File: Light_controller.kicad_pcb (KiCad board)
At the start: 2 copper layers, 42 parts, among them U1 LM358, U10 PH2.0_horizontal, U11 PH2.0_horizontal, U12 PH2.0_horizontal, U13 PinSocket_1x4, U14 SMD2063, U2 PT8211-S, U3 STM8S003F3P, U4 SMD_2062, U5 tact_sw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

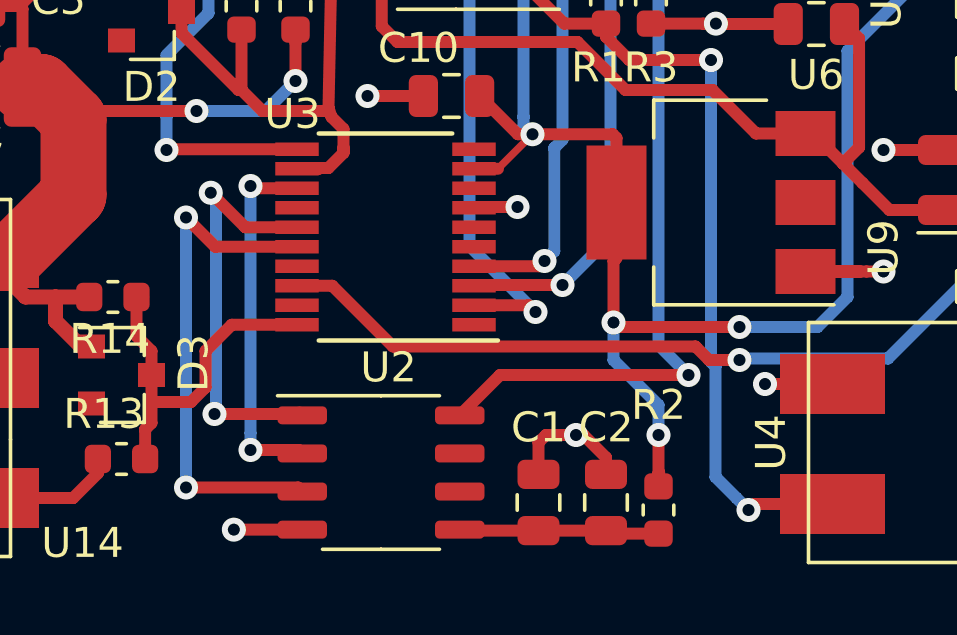
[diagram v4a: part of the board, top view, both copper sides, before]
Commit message: updated layout
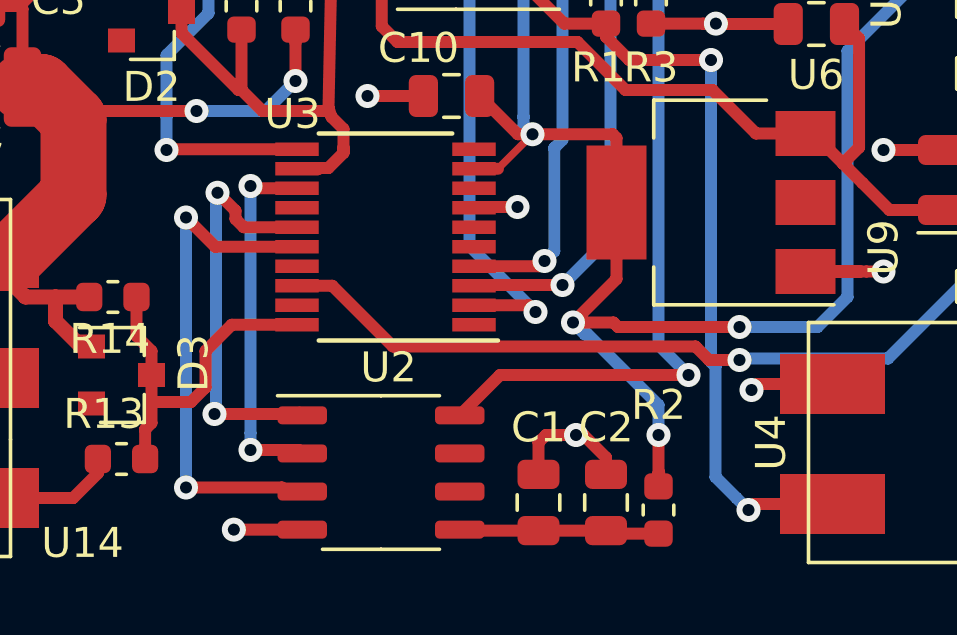
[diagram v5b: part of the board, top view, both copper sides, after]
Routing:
- net /5V_SUPPLY: track 101.5 -> 106.2 mm

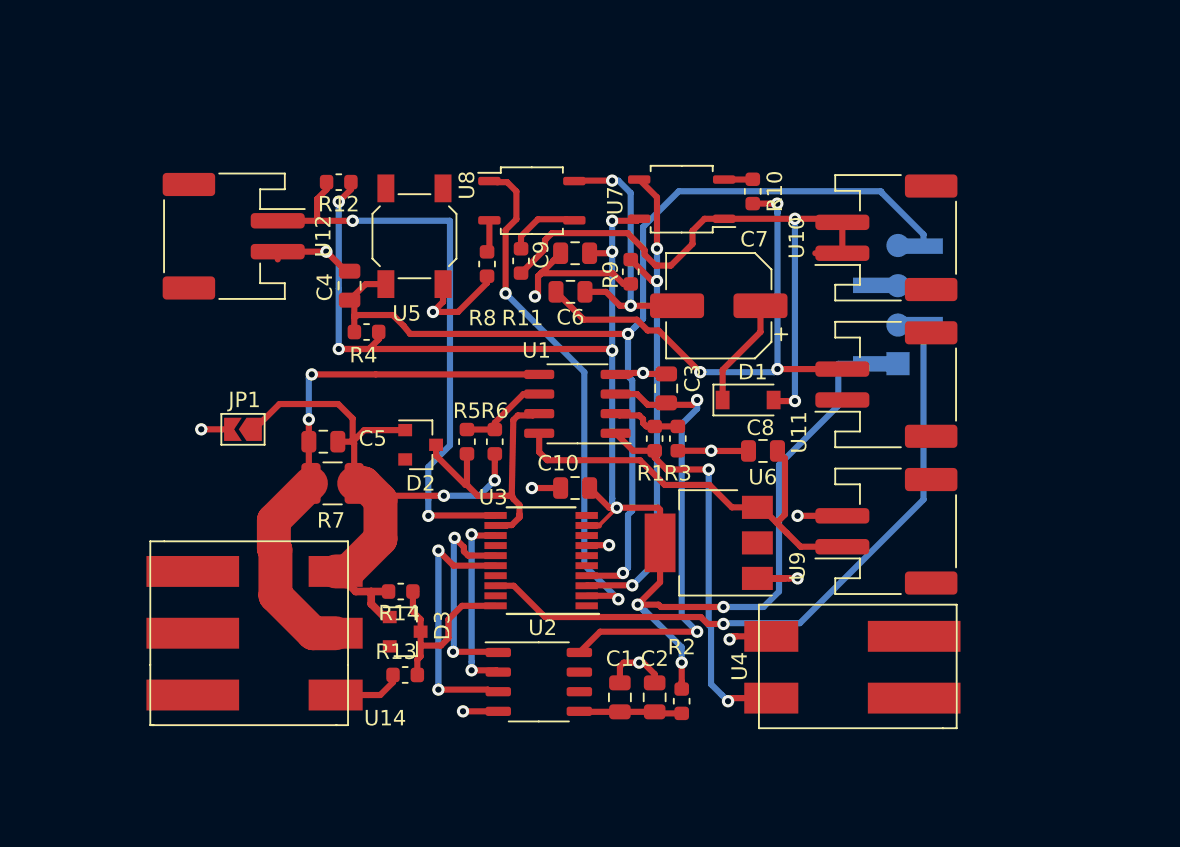
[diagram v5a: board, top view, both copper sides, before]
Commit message: updated circuit with larger trace on high current
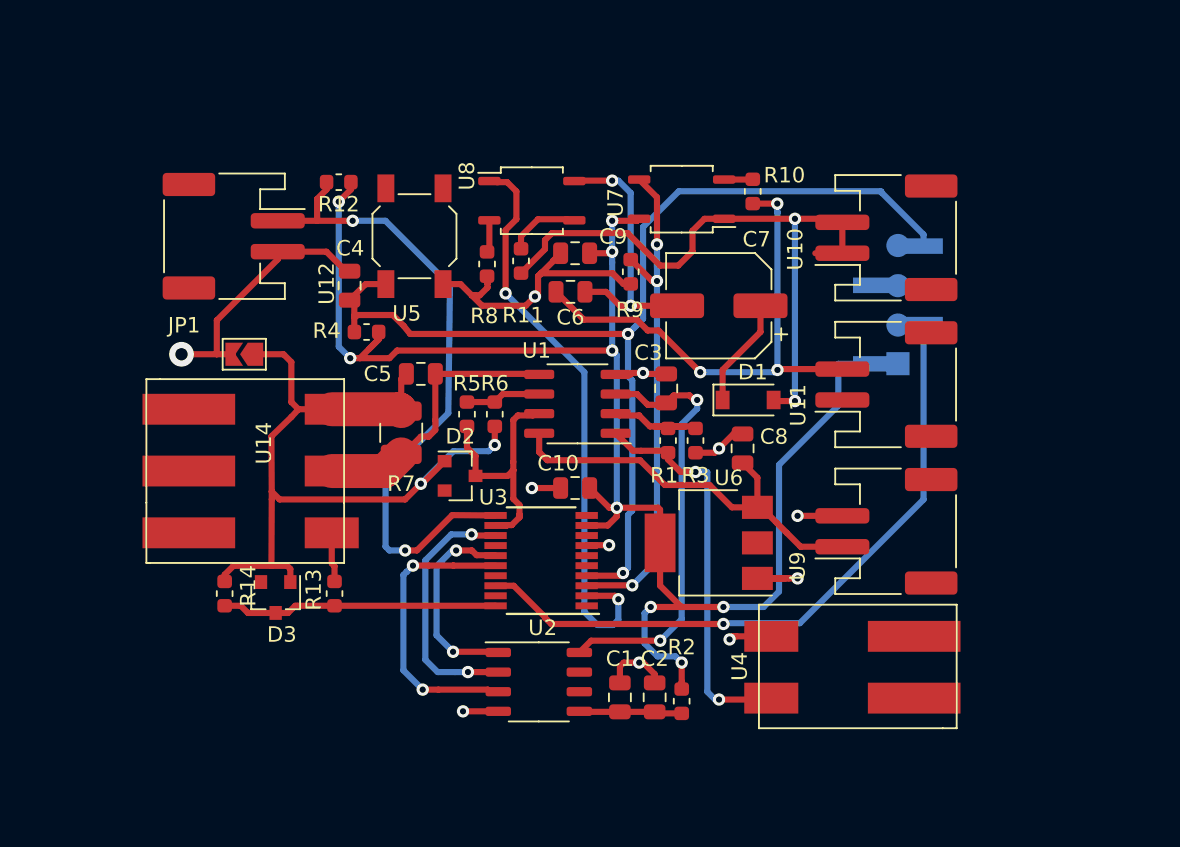
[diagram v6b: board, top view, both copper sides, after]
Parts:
- moved R14 11.4 mm to (137.4, 81.5), turned to 90 degrees
- moved U14 10.5 mm to (136.5, 63.5)
- moved D3 8.67 mm to (140.7, 81.8), turned to 270 degrees
- moved C5 7.69 mm to (150.1, 67.3), turned to 180 degrees
- moved R13 6.98 mm to (144.5, 81.5), turned to 270 degrees
- moved R7 5.52 mm to (148.8, 71.1), turned to 270 degrees
- moved JP1 4.86 mm to (138.7, 66.0)
- moved D2 3.25 mm to (152.7, 73.9)
- moved R5 1.78 mm to (153.1, 69.9)
- moved R6 1.78 mm to (154.9, 69.9)
- moved C8 1.33 mm to (170.9, 72.1), turned to 90 degrees
- moved R3 1.15 mm to (167.9, 71.6)
- moved R1 0.88 mm to (166.1, 71.6)
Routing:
- net /LED_SENSE: track 35.5 -> 18.2 mm, vias 2 -> 0
- net GND: track 52.6 -> 63.0 mm, vias 13 -> 11
- net /LED-: track 40.9 -> 51.3 mm
- net /V_SENSOR: track 12.9 -> 17.9 mm
- net /TEMP_SENSOR: track 37.9 -> 42.7 mm
- net /WS: track 12.3 -> 16.8 mm
- net /UART_TX: track 33.9 -> 37.8 mm
- net Net-(R1-Pad1): track 4.51 -> 7.56 mm
- net /SPI_MOSI: track 16.8 -> 19.1 mm
- net /RCH: track 29.7 -> 27.5 mm
- net /C_SENSOR: track 19.0 -> 16.9 mm
- net /LED+: track 5.02 -> 3.22 mm
- net /12V_INPUT: track 28.6 -> 26.8 mm
- net Net-(R5-Pad1): track 5.89 -> 4.91 mm

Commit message: modified the custom footprint, finalized the schematic and layout of the pcb design for stm8
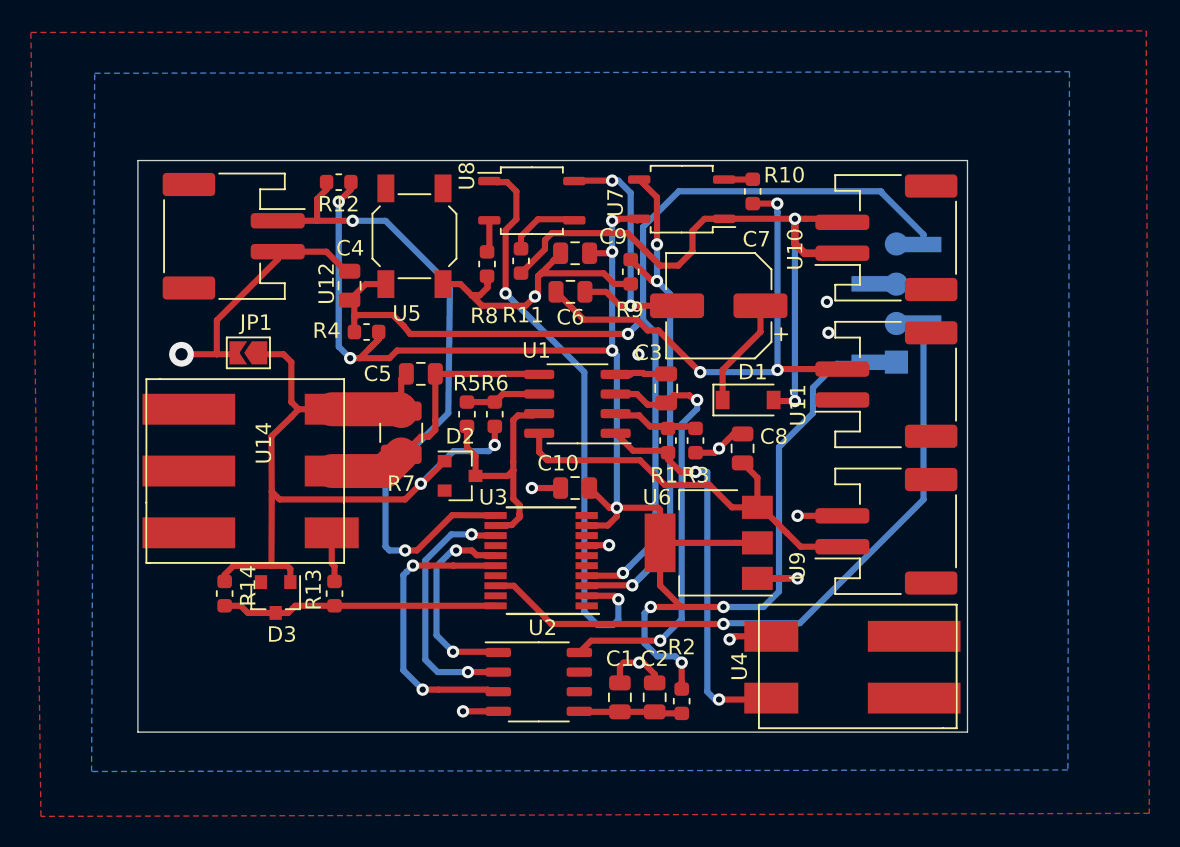
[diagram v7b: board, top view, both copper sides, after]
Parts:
- moved JP1 0.28 mm to (138.9, 66.0)
- moved U13 0.14 mm to (180.9, 72.2)
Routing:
- net /5V_SUPPLY: track 106.2 -> 114.4 mm
- net /RESET: track 71.1 -> 75.1 mm
- net /UART_RX: track 32.9 -> 35.4 mm
- net /SWIM: track 43.4 -> 45.1 mm
- net GND: track 63.0 -> 64.4 mm, vias 11 -> 13
- net /RX_in: track 42.2 -> 43.4 mm
- added copper zone on B.Cu, net GND
- added copper zone on F.Cu, net GND
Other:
- board outline added: 53.7 x 37 mm
